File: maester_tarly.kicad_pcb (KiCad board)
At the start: 4 copper layers, 126 parts, among them J101 Micro_SD_Card_Det, J102 USB_B_Micro, J103 USB_A, J104 Conn_01x06, J105 Conn_01x10, J106 RJ45_Amphenol_RJMG1BD3B8K1ANR, J107 DF40GB(1.5)-48DS-0.4V, J108 DF40GB(1.5)-48DS-0.4V, J109 DF40GB(1.5)-48DS-0.4V, J110 DF40GB(1.5)-48DS-0.4V, U1 SAM9X60, U2 W971GG6SB-18, U3 MCP16501, U501 KSZ8081RNA, Y401 32.768kHz, Y402 DSC1001, Y501 DSC1001

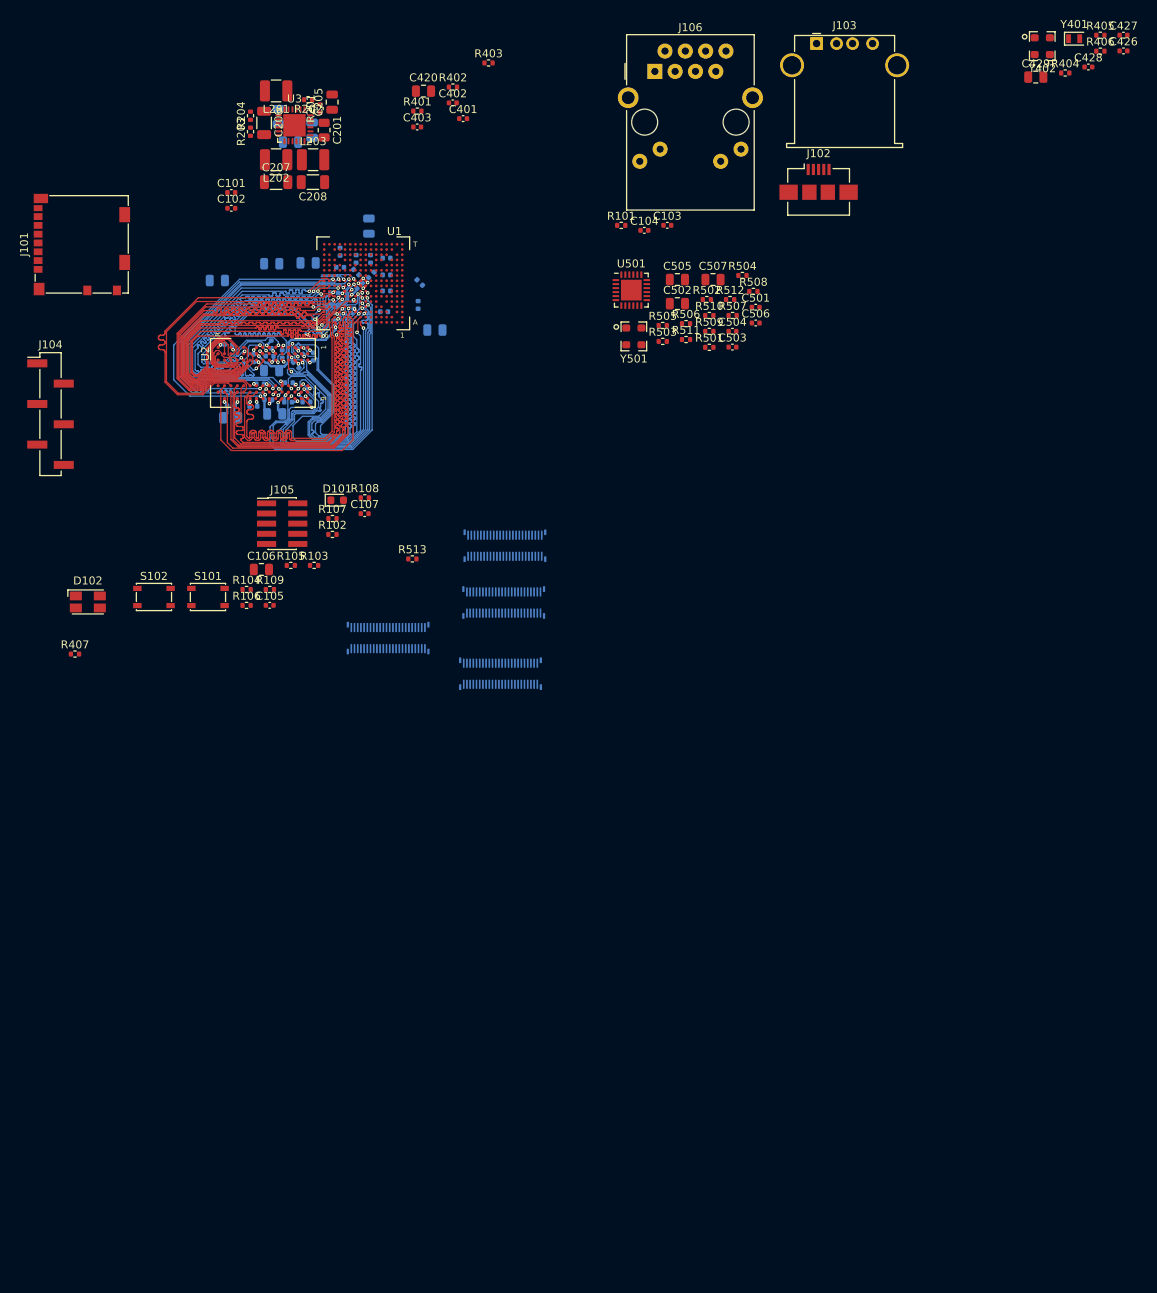
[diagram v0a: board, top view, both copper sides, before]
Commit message: Escaped all traced from the CPU
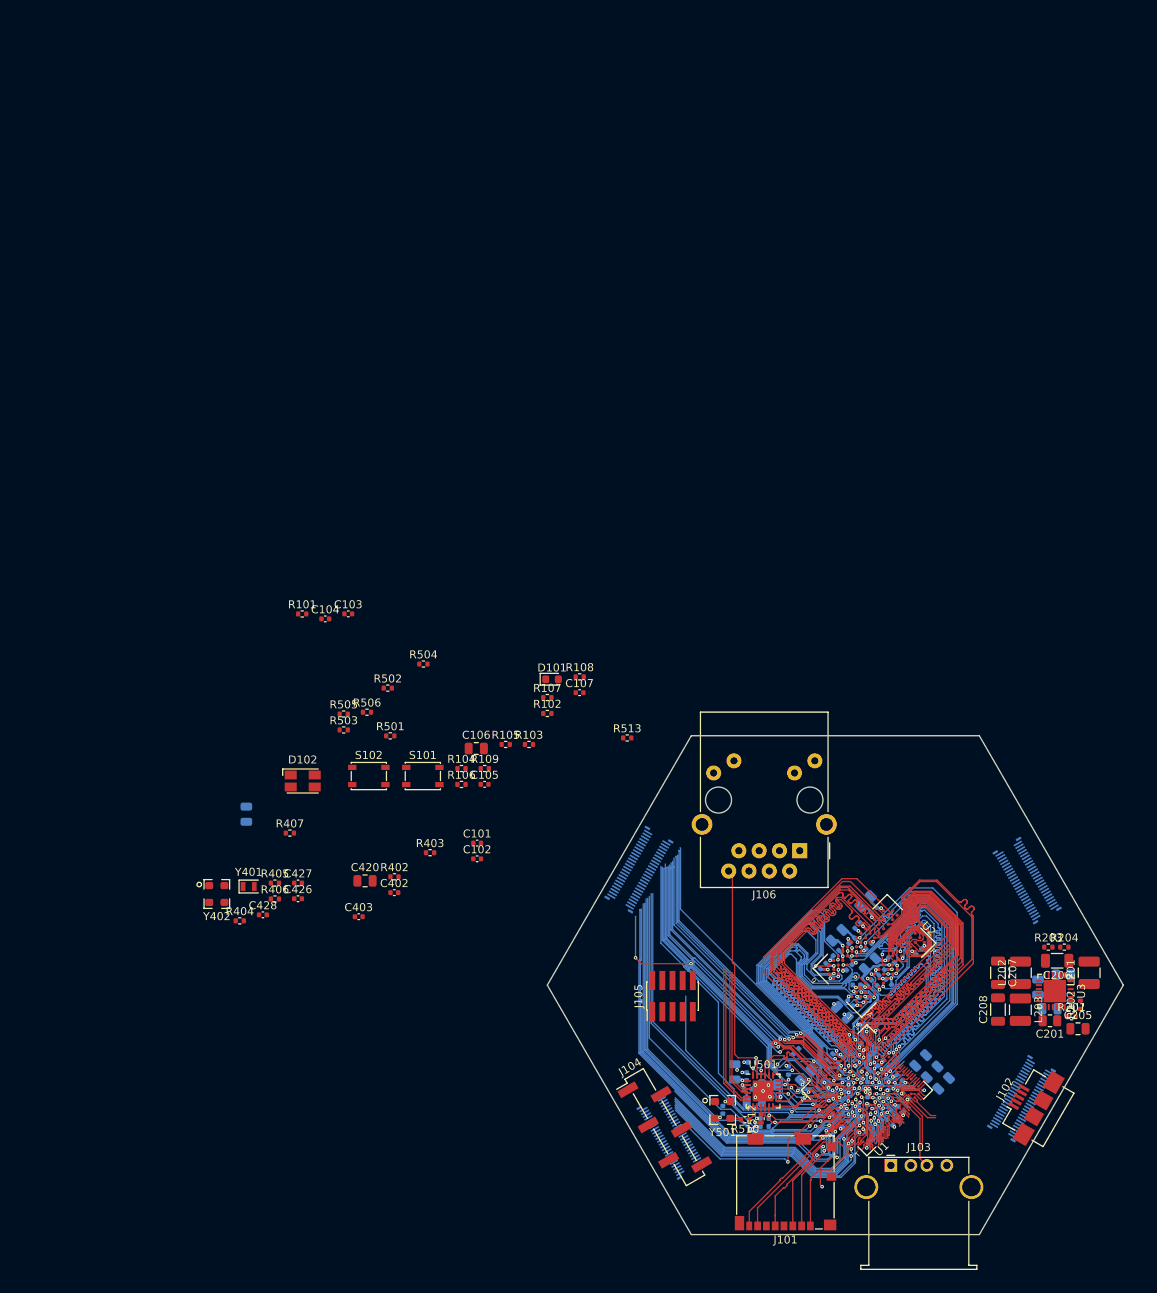
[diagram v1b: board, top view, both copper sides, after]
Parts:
- C401, C429, C501, C502, C503, C504, C505, C506, C507, R401, R507, R508, R509, R511: moved to B.Cu
- moved L201 149.9 mm to (149.7, 129.6), turned to 90 degrees
- moved R202 148.7 mm to (148.6, 133.6), turned to 90 degrees
- moved C205 148.7 mm to (148.3, 136.6), turned to 0 degrees
- moved R404 147.9 mm to (43.6, 123.1)
- moved C426 147.9 mm to (50.8, 120.4)
- moved C427 147.9 mm to (50.8, 118.4)
- moved C428 147.9 mm to (46.5, 122.4)
- moved R405 147.9 mm to (48.0, 118.4)
- moved R406 147.9 mm to (48.0, 120.4)
- moved Y401 147.9 mm to (44.7, 118.8)
- moved Y402 147.9 mm to (40.7, 119.8)
- moved R201 147.3 mm to (147.5, 135.1), turned to 0 degrees
- moved J101 146.6 mm to (111.8, 155.8), turned to 180 degrees
- moved R204 145.4 mm to (146.6, 126.4), turned to 0 degrees
- moved C202 145.4 mm to (146.5, 129.9), turned to 180 degrees
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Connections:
- J101 pad 10: Net-(J101-Pad10) -> (no net)
- J101 pad 9: Net-(J101-Pad9) -> (no net)
- J102 pad 4: Net-(J102-Pad4) -> (no net)
- J104 pad 1: Net-(J104-Pad1) -> (no net)
- J104 pad 4: Net-(J104-Pad4) -> (no net)
- J104 pad 5: Net-(J104-Pad5) -> (no net)
- J105 pad 7: Net-(J105-Pad7) -> (no net)
- J105 pad 9: Net-(J105-Pad9) -> (no net)
- J106 pad L3: Net-(J106-PadL3) -> (no net)
- J106 pad L4: Net-(J106-PadL4) -> (no net)
- J106 pad R7: Net-(J106-PadR7) -> (no net)
- J107 pad 10: /a2 -> /c24
- J107 pad 12: /a3 -> /c25
- J107 pad 14: /a4 -> /c26
- J107 pad 16: /a5 -> /c27
- J107 pad 18: /a6 -> /c28
- J107 pad 20: /a7 -> /c29
- J107 pad 22: /a12 -> /c30
- J107 pad 24: /a13 -> /c31
- J107 pad 26: /a14 -> /a21
- J107 pad 28: /a21 -> /a14
- J107 pad 30: /a22 -> /a13
- J107 pad 32: /a23 -> /a12
- J107 pad 34: /a24 -> /a7
- J107 pad 36: /a25 -> /a6
- J107 pad 38: /a26 -> /a5
- J107 pad 40: /a27 -> /a4
- J107 pad 42: /a28 -> /a3
- J107 pad 44: /a29 -> /a2
- J107 pad 46: /a30 -> /a1
- J107 pad 48: /a31 -> /a0
- J107 pad 6: /a0 -> /c22
- J107 pad 8: /a1 -> /c23
- J109 pad 10: /b15 -> /a27
- J109 pad 12: /b16 -> /a26
- J109 pad 14: /b17 -> /a25
- J109 pad 16: /b18 -> /a24
- J109 pad 18: /b19 -> /a23
- J109 pad 2: /b11 -> /a31
- J109 pad 20: /b20 -> /a22
- J109 pad 22: /b21 -> /b11
- J109 pad 24: /b22 -> /b12
- J109 pad 26: /b23 -> /b13
- J109 pad 28: /b24 -> /b14
- J109 pad 30: /c22 -> /b15
- J109 pad 32: /c23 -> /b16
- J109 pad 34: /c24 -> /b17
- J109 pad 36: /c25 -> /b18
- J109 pad 38: /c26 -> /b19
- J109 pad 4: /b12 -> /a30
- J109 pad 40: /c27 -> /b20
- J109 pad 42: /c28 -> /b21
- J109 pad 44: /c29 -> /b22
- J109 pad 46: /c30 -> /b23
- J109 pad 48: /c31 -> /b24
- J109 pad 6: /b13 -> /a29
- J109 pad 8: /b14 -> /a28
- U1 pad A10: Net-(U1-PadA10) -> (no net)
- U1 pad A11: Net-(U1-PadA11) -> (no net)
- U1 pad B10: Net-(U1-PadB10) -> (no net)
- U1 pad E8: Net-(U1-PadE8) -> (no net)
- U1 pad F12: Net-(U1-PadF12) -> (no net)
- U1 pad F15: Net-(U1-PadF15) -> (no net)
- U1 pad G15: Net-(U1-PadG15) -> (no net)
- U1 pad G16: Net-(U1-PadG16) -> (no net)
- U1 pad H14: Net-(U1-PadH14) -> (no net)
- U1 pad L14: Net-(U1-PadL14) -> (no net)
- U1 pad N12: Net-(U1-PadN12) -> (no net)
- U1 pad P12: Net-(U1-PadP12) -> (no net)
- U1 pad P9: Net-(U1-PadP9) -> (no net)
- U2 pad A2: Net-(U2-PadA2) -> (no net)
- U2 pad E2: Net-(U2-PadE2) -> (no net)
- U2 pad R3: Net-(U2-PadR3) -> (no net)
- U2 pad R7: Net-(U2-PadR7) -> (no net)
- U2 pad R8: Net-(U2-PadR8) -> (no net)
- U3 pad 15: Net-(U3-Pad15) -> (no net)
- U501 pad 8: Net-(U501-Pad8) -> (no net)
- Y402 pad 1: Net-(Y402-Pad1) -> (no net)
- Y501 pad 1: Net-(Y501-Pad1) -> (no net)
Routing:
- net /a23: track 0.00 -> 55.1 mm, vias 0 -> 1
- net /a31: track 0.00 -> 50.3 mm, vias 0 -> 1
- net /a29: track 0.00 -> 49.8 mm, vias 0 -> 1
- net /a12: track 0.00 -> 49.4 mm, vias 0 -> 1
- net /a27: track 0.00 -> 48.6 mm, vias 0 -> 1
- net /a25: track 0.00 -> 48.4 mm, vias 0 -> 1
- net /a24: track 0.33 -> 48.7 mm
- net /a30: track 0.00 -> 47.3 mm, vias 0 -> 1
- net /b14: track 0.00 -> 46.4 mm, vias 0 -> 1
- net /a22: track 0.00 -> 45.8 mm, vias 0 -> 1
- net /b17: track 0.00 -> 43.8 mm, vias 0 -> 1
- net /a21: track 0.00 -> 42.8 mm, vias 0 -> 3
- net /b15: track 0.00 -> 39.2 mm, vias 0 -> 1
- net /b12: track 0.00 -> 39.1 mm, vias 0 -> 1
- net /CPU_CORE/CPU_JTAG_TDO: track 0.00 -> 39.0 mm, vias 0 -> 1
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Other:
- board outline added: 72 x 62.4 mm

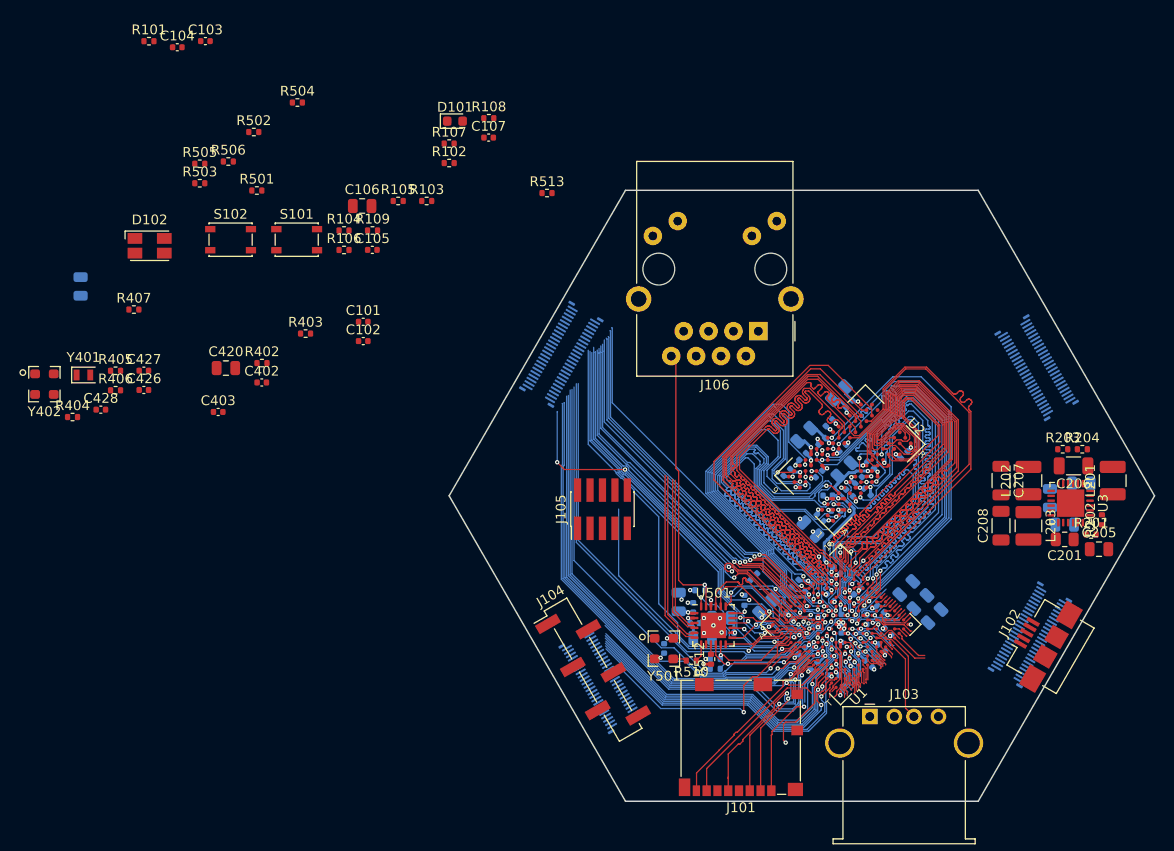
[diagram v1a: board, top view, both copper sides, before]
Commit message: Placed all the parts. Some will have to move.
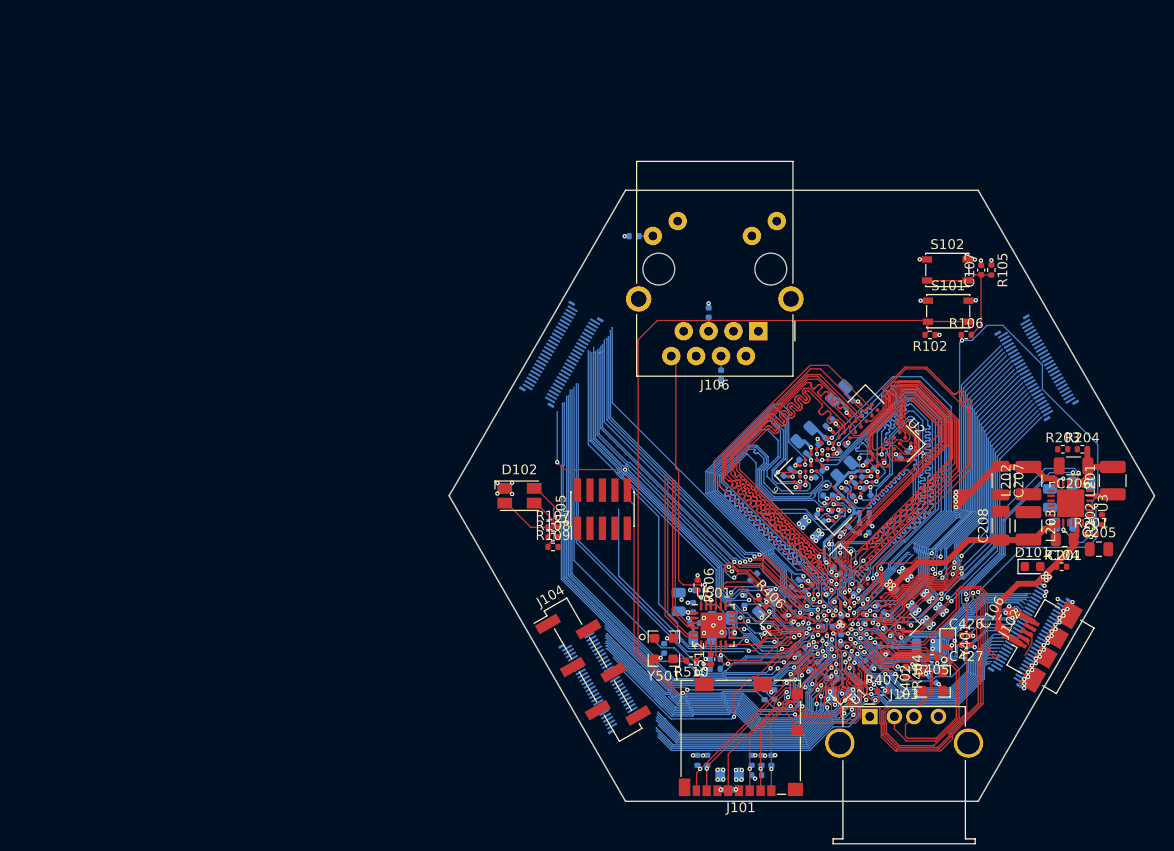
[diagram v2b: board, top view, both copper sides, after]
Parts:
- C101, C103, C104, C105, C402, C403, C420, C428, R101, R103, R402, R403, R501, R502, R503, R504, R505, R513: moved to B.Cu
- C102: footprint Capacitor_SMD:C_0402_1005Metric -> Capacitor_SMD:C_0805_2012Metric; moved to B.Cu
- moved Y402 95.6 mm to (131.3, 150.1), turned to 270 degrees
- moved Y401 92.3 mm to (132.9, 145.9), turned to 270 degrees
- moved C428 89.3 mm to (131.4, 149.9), turned to 315 degrees
- moved R404 88.9 mm to (128.6, 149.1), turned to 270 degrees
- moved C427 88.5 mm to (134.8, 146.4), turned to 180 degrees
- moved R405 88.4 mm to (131.3, 147.8), turned to 180 degrees
- moved C404 88.1 mm to (122.1, 151.4), turned to 0 degrees
- moved C426 87.6 mm to (134.8, 145.4)
- moved R407 85.8 mm to (126.2, 151.1)
- moved R505 83.6 mm to (113.9, 158.2), turned to 270 degrees
- moved R504 82.8 mm to (114.9, 158.2), turned to 270 degrees
- moved R104 80.9 mm to (144.5, 138.4)
- moved R502 79.1 mm to (108.3, 158.2), turned to 270 degrees
- moved C106 78.2 mm to (138.9, 143.9), turned to 60 degrees
- moved R503 77.8 mm to (107.3, 158.2), turned to 270 degrees
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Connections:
- J101 pad 10: (no net) -> Net-(J101-Pad10)
- J101 pad 9: (no net) -> Net-(J101-Pad9)
- J102 pad 4: (no net) -> Net-(J102-Pad4)
- J104 pad 1: (no net) -> Net-(J104-Pad1)
- J104 pad 4: (no net) -> Net-(J104-Pad4)
- J104 pad 5: (no net) -> Net-(J104-Pad5)
- J105 pad 7: (no net) -> Net-(J105-Pad7)
- J105 pad 9: (no net) -> Net-(J105-Pad9)
- J106 pad L3: (no net) -> Net-(J106-PadL3)
- J106 pad L4: (no net) -> Net-(J106-PadL4)
- J106 pad R7: (no net) -> Net-(J106-PadR7)
- J107 pad 10: /c24 -> /c2
- J107 pad 12: /c25 -> /c3
- J107 pad 14: /c26 -> /c4
- J107 pad 16: /c27 -> /c5
- J107 pad 18: /c28 -> /c6
- J107 pad 20: /c29 -> /c7
- J107 pad 22: /c30 -> /c8
- J107 pad 24: /c31 -> /c9
- J107 pad 6: /c22 -> /c0
- J107 pad 8: /c23 -> /c1
- J108 pad 10: /c2 -> /c12
- J108 pad 12: /c3 -> /c13
- J108 pad 14: /c4 -> /c14
- J108 pad 16: /c5 -> /c15
- J108 pad 18: /c6 -> /c16
- J108 pad 20: /c7 -> /c17
- J108 pad 22: /c8 -> /c18
- J108 pad 24: /c9 -> /c19
- J108 pad 26: /c10 -> /c20
- J108 pad 28: /c11 -> /c21
- J108 pad 30: /c12 -> /c22
- J108 pad 32: /c13 -> /c23
- J108 pad 34: /c14 -> /c24
- J108 pad 36: /c15 -> /c25
- J108 pad 38: /c16 -> /c26
- J108 pad 40: /c17 -> /c27
- J108 pad 42: /c18 -> /c28
- J108 pad 44: /c19 -> /c29
- J108 pad 46: /c20 -> /c30
- J108 pad 48: /c21 -> /c31
- J108 pad 6: /c0 -> /c10
- J108 pad 8: /c1 -> /c11
- U1 pad A10: (no net) -> Net-(U1-PadA10)
- U1 pad A11: (no net) -> Net-(U1-PadA11)
- U1 pad B10: (no net) -> Net-(U1-PadB10)
- U1 pad E8: (no net) -> Net-(U1-PadE8)
- U1 pad F12: (no net) -> Net-(U1-PadF12)
- U1 pad F15: (no net) -> Net-(U1-PadF15)
- U1 pad G15: (no net) -> Net-(U1-PadG15)
- U1 pad G16: (no net) -> Net-(U1-PadG16)
- U1 pad H14: (no net) -> Net-(U1-PadH14)
- U1 pad L14: (no net) -> Net-(U1-PadL14)
- U1 pad N12: (no net) -> Net-(U1-PadN12)
- U1 pad P12: (no net) -> Net-(U1-PadP12)
- U1 pad P9: (no net) -> Net-(U1-PadP9)
- U2 pad A2: (no net) -> Net-(U2-PadA2)
- U2 pad E2: (no net) -> Net-(U2-PadE2)
- U2 pad R3: (no net) -> Net-(U2-PadR3)
- U2 pad R7: (no net) -> Net-(U2-PadR7)
- U2 pad R8: (no net) -> Net-(U2-PadR8)
- U3 pad 15: (no net) -> Net-(U3-Pad15)
- U501 pad 8: (no net) -> Net-(U501-Pad8)
- Y402 pad 1: (no net) -> Net-(Y402-Pad1)
- Y501 pad 1: (no net) -> Net-(Y501-Pad1)
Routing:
- net +5V: track 0.00 -> 105.3 mm, vias 0 -> 4
- net /cpu_reset: track 0.60 -> 93.7 mm, vias 0 -> 4
- net Net-(C105-Pad1): track 0.00 -> 84.0 mm, vias 0 -> 1
- net /start_btn: track 7.98 -> 73.6 mm, vias 1 -> 3
- net /CPU_CORE/CPU_SHUTDOWN: track 2.07 -> 60.3 mm, vias 0 -> 2
- net /d5: track 3.55 -> 61.5 mm, vias 0 -> 2
- net /ldo_en: track 9.35 -> 65.2 mm, vias 1 -> 2
- net /CPU_CORE/CPU_WAKEUP: track 1.09 -> 55.8 mm, vias 0 -> 2
- net +1.15V: track 2.03 -> 41.4 mm, vias 3 -> 7
- net /d20: track 3.45 -> 37.9 mm
- net /d11: track 5.00 -> 36.7 mm
- net /d9: track 4.72 -> 36.4 mm
- net /d18: track 2.79 -> 34.2 mm
- net /d14: track 3.66 -> 35.0 mm
- net /d13: track 1.11 -> 32.4 mm, vias 0 -> 1
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- added copper zone on In2.Cu, net +1.15V
- added copper zone on In2.Cu, net +1.8V
- added copper zone on In2.Cu, net +3V3
- added copper zone on In1.Cu, net GND
